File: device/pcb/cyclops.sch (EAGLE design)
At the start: 199 parts, among them Q1 NDS351AN, Q2 NDS351AN, Q3 NDS351AN, Q4 IRF510, U1 MCP4921, U10 LT1880, U11 ZXTD, U12 ADG1201, U13 THS4281, U14 ZXTD, U16 OPA1664, U2 LT1764A, U3 BD00FC0WEFJ, U4 LTM8020, U5 LT1931, U6 TPS72325, U7 TLV3701, U75 TXB0104RGYR, U8 LT1711, U9 ADR03

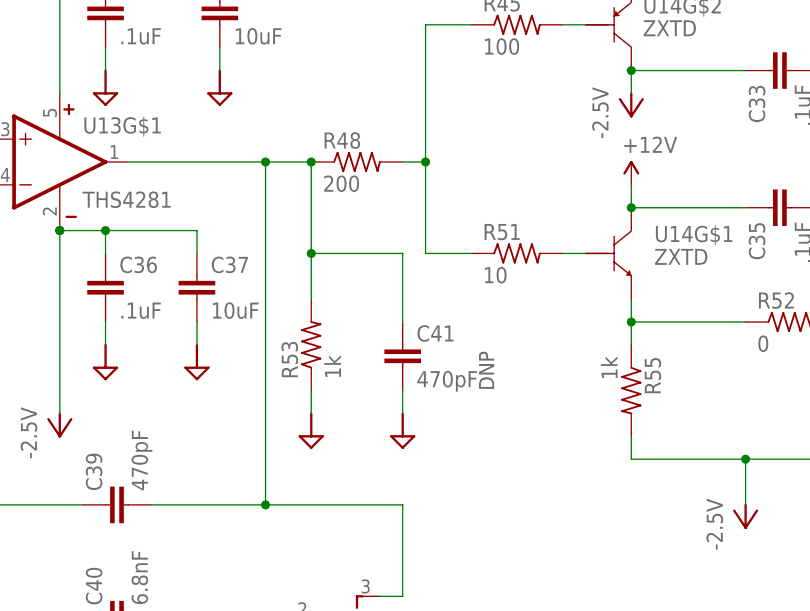
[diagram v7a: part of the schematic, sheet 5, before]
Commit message: Compensation capacitor to silince ringing in BJT booster stage
- Seems to cure all ringing for different LEDs and cable lengths
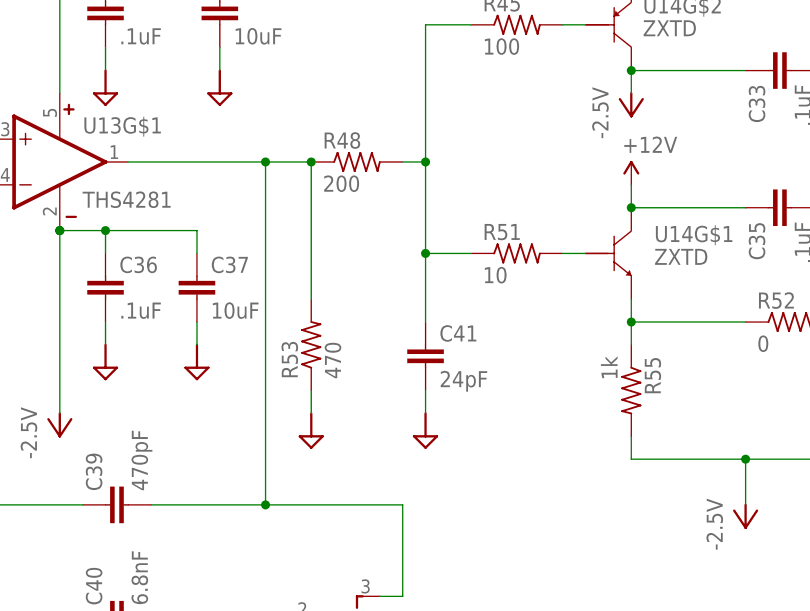
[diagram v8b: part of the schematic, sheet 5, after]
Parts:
- C41: value 470pF -> 24pF
- R53: value 1k -> 470
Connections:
- removed net N$16: R45.1, R48.2, R51.1
- new net N$58: C41.1, R45.1, R48.2, R51.1
- net N$13: no longer C41.1
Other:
- moved on the sheet: C41
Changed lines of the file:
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@@
 <part name="R45" library="cyclops" deviceset="R" device="_0603" value="100"/>
 <part name="R51" library="cyclops" deviceset="R" device="_0603" value="10"/>
-<part name="R53" library="cyclops" deviceset="R" device="_0603" value="1k"/>
+<part name="R53" library="cyclops" deviceset="R" device="_0603" value="470"/>
 <part name="U$45" library="cyclops" deviceset="GND2" device=""/>
 <part name="C29" library="jonnew" deviceset="C" device="_0603" value=".1uF"/>
@@
 <part name="D7" library="jonnew" deviceset="S-DIODE" device="SOD-123" value="1N5819"/>
 <part name="U$13" library="cyclops" deviceset="GND2" device=""/>
-<part name="C41" library="cyclops" deviceset="C" device="_0603" value="470pF"/>
+<part name="C41" library="cyclops" deviceset="C" device="_0603" value="24pF"/>
 <part name="U$12" library="cyclops" deviceset="GND2" device=""/>
 </parts>
@@
 <text x="-7.62" y="124.46" size="1.6764" layer="97" rot="R90">DNP</text>
 <text x="-20.32" y="119.38" size="1.6764" layer="97" rot="R90">DNP</text>
-<text x="73.66" y="73.66" size="1.6764" layer="97" rot="R90">DNP</text>
 </plain>
 <instances>
@@
 <instance part="D7" gate="G$1" x="15.24" y="20.32" rot="R90"/>
 <instance part="U$13" gate="G$1" x="17.78" y="7.62"/>
-<instance part="C41" gate="C" x="63.5" y="78.74"/>
-<instance part="U$12" gate="G$1" x="63.5" y="68.58" rot="MR0"/>
+<instance part="C41" gate="C" x="66.04" y="78.74"/>
+<instance part="U$12" gate="G$1" x="66.04" y="68.58" rot="MR0"/>
 </instances>
 <busses>
@@
 <segment>
 <pinref part="C41" gate="C" pin="2"/>
-<wire x1="63.5" y1="73.66" x2="63.5" y2="71.12" width="0.1524" layer="91"/>
+<wire x1="66.04" y1="73.66" x2="66.04" y2="71.12" width="0.1524" layer="91"/>
 </segment>
 </net>
@@
 <junction x="48.26" y="60.96"/>
 <pinref part="R53" gate="R" pin="2"/>
-<wire x1="53.34" y1="83.82" x2="53.34" y2="88.9" width="0.1524" layer="91"/>
 <junction x="53.34" y="99.06"/>
 <pinref part="LIM&lt;BW&gt;FULL" gate="G$1" pin="3"/>
-<wire x1="53.34" y1="88.9" x2="53.34" y2="99.06" width="0.1524" layer="91"/>
+<wire x1="53.34" y1="83.82" x2="53.34" y2="99.06" width="0.1524" layer="91"/>
 <wire x1="60.96" y1="50.8" x2="63.5" y2="50.8" width="0.1524" layer="91"/>
 <wire x1="63.5" y1="50.8" x2="63.5" y2="60.96" width="0.1524" layer="91"/>
-<wire x1="53.34" y1="88.9" x2="63.5" y2="88.9" width="0.1524" layer="91"/>
-<wire x1="63.5" y1="88.9" x2="63.5" y2="81.28" width="0.1524" layer="91"/>
-<junction x="53.34" y="88.9"/>
-<pinref part="C41" gate="C" pin="1"/>
 </segment>
 </net>
@@
 </segment>
 </net>
-<net name="N$16" class="0">
-<segment>
-<pinref part="R48" gate="R" pin="2"/>
-<wire x1="63.5" y1="99.06" x2="66.04" y2="99.06" width="0.1524" layer="91"/>
-<pinref part="R45" gate="R" pin="1"/>
-<wire x1="71.12" y1="114.3" x2="66.04" y2="114.3" width="0.1524" layer="91"/>
-<wire x1="66.04" y1="114.3" x2="66.04" y2="99.06" width="0.1524" layer="91"/>
-<pinref part="R51" gate="R" pin="1"/>
-<wire x1="71.12" y1="88.9" x2="66.04" y2="88.9" width="0.1524" layer="91"/>
-<wire x1="66.04" y1="88.9" x2="66.04" y2="99.06" width="0.1524" layer="91"/>
-<junction x="66.04" y="99.06"/>
-</segment>
-</net>
 <net name="N$40" class="0">
 <segment>
@@
 </segment>
 </net>
+<net name="N$58" class="0">
+<segment>
+<wire x1="66.04" y1="88.9" x2="66.04" y2="81.28" width="0.1524" layer="91"/>
+<pinref part="C41" gate="C" pin="1"/>
+<pinref part="R48" gate="R" pin="2"/>
+<wire x1="63.5" y1="99.06" x2="66.04" y2="99.06" width="0.1524" layer="91"/>
+<pinref part="R45" gate="R" pin="1"/>
+<wire x1="71.12" y1="114.3" x2="66.04" y2="114.3" width="0.1524" layer="91"/>
+<wire x1="66.04" y1="114.3" x2="66.04" y2="99.06" width="0.1524" layer="91"/>
+<pinref part="R51" gate="R" pin="1"/>
+<wire x1="71.12" y1="88.9" x2="66.04" y2="88.9" width="0.1524" layer="91"/>
+<wire x1="66.04" y1="88.9" x2="66.04" y2="99.06" width="0.1524" layer="91"/>
+<junction x="66.04" y="99.06"/>
+<junction x="66.04" y="88.9"/>
+</segment>
+</net>
